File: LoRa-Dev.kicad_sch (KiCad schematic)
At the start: 14 parts, among them J2 Barrel_Jack_MountingPin, U1 RPi Pico, U2 LT1963AEQ

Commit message: board layout
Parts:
- added C3: 47uF, Capacitor_SMD:CP_Elec_6.3x5.8, symbol Device:C_Polarized_Small
- added C4: 0.1uF, Capacitor_SMD:C_0603_1608Metric, symbol Device:C_Small
- added J1: Conn_Coaxial_Small, Connector_Coaxial:U.FL_Hirose_U.FL-R-SMT-1_Vertical, symbol Connector:Conn_Coaxial_Small
- added R9: R_Small, Resistor_SMD:R_0603_1608Metric, symbol Device:R_Small
- added U3: LoRa126XF30, LoRa-Dev:LoRa126XF30, symbol LoRa-Dev:LoRa126XF30
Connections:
- net GND: now also J2.MP (MountPin), C3.2, C4.2, R9.2, U3.2 (GND), U3.8 (GND)
- net RF_VDD: now also C3.1, C4.1, U3.1 (VCC)
- net SPI_CSn: now also U3.7 (NSS)
- net SPI_MISO: now also U3.10 (MISO)
- net SPI_MOSI: now also U3.11 (MOSI)
- net SPI_SCK: now also U3.9 (SCK)
- net 12V: now reaches J2.1, R1.1, R2.1, R3.1, R4.1, R5.1, R6.1
- net DIO3: now reaches U1.26 (GP20)
- net DIO3: now also U3.14 (DIO3)
- net DIO1: now reaches U1.27 (GP21)
- net DIO1: now also U3.13 (DIO1)
- net RESETn: now reaches U1.29 (GP22)
- net RESETn: now also U3.5 (NRESET)
- net BUSY: now reaches U1.31 (GP26)
- net BUSY: now also U3.6 (BUSY)
- new net ANT: J1.1 (In), U3.16 (ANT)
- new net RF_GND: J1.2 (Ext), R9.1, U3.15 (GND)
- no-connect marks 0 -> 3

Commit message: RFM95W
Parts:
- removed C3: 47uF, Capacitor_SMD:CP_Elec_6.3x5.8, symbol Device:C_Polarized_Small
- removed C4: 0.1uF, Capacitor_SMD:C_0603_1608Metric, symbol Device:C_Small
- removed U3: LoRa126XF30, LoRa-Dev:LoRa126XF30, symbol LoRa-Dev:LoRa126XF30
- added C3: 0.1uF, Capacitor_SMD:C_0603_1608Metric, symbol Device:C_Small
- added C4: 47uF, Capacitor_SMD:CP_Elec_6.3x5.8, symbol Device:C_Polarized_Small
- added U5: RFM95W-868S2, LoRa-Dev:RFM95W, symbol RF_Module:RFM95W-868S2
- R7: value 1k5 -> 2K2
- R8: value 4k7 -> 1K2
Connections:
- net ANT: now also U5.9 (ANT)
- net DIO1: now also U5.15 (DIO1)
- net GND: now also C3.2, C4.2, U5.1 (GND), U5.10 (GND), U5.8 (GND)
- net RESETn: now also U5.6 (RESET)
- net RF_VDD: now also C3.1, C4.1, U5.13 (3.3V)
- net SPI_CSn: now also U5.5 (NSS)
- net SPI_MISO: now also U5.2 (MISO)
- net SPI_MOSI: now also U5.3 (MOSI)
- net SPI_SCK: now also U5.4 (SCK)
- net BUSY: no longer names the net of U1.31 (GP26)
- net DIO3 renamed DIO0
- net DIO0: now also U5.14 (DIO0)
- no-connect marks 3 -> 4

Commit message: RFM95PW wrong branch name
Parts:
- removed J1: Conn_Coaxial_Small, Connector_Coaxial:U.FL_Hirose_U.FL-R-SMT-1_Vertical, symbol Connector:Conn_Coaxial_Small
- removed U5: RFM95W-868S2, LoRa-Dev:RFM95W, symbol RF_Module:RFM95W-868S2
- added J3: Conn_Coaxial_Small, Connector_Coaxial:U.FL_Hirose_U.FL-R-SMT-1_Vertical, symbol Connector:Conn_Coaxial_Small
- added U3: RFM95PW, LoRa-Dev:RFM95PW, symbol LoRa-Dev:RFM95PW
- R7: value 2K2 -> 4k7
- R8: value 1K2 -> 1K5
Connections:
- net ANT: now also J3.1 (In), U3.1 (ANT)
- net DIO0: now also U3.6 (DIO0)
- net DIO1: now also U3.7 (DIO1)
- net GND: now also U3.16 (GND), U3.17 (GND), U3.2 (GND)
- net RESETn: now also U3.14 (RESET)
- net RF_GND: now also J3.2 (Ext)
- net RF_VDD: now also U3.5 (VCC)
- net SPI_CSn: now also U3.13 (NSS)
- net SPI_MISO: now also U3.10 (MISO)
- net SPI_MOSI: now also U3.11 (MOSI)
- net SPI_SCK: now also U3.12 (SCK)
- no-connect marks 4 -> 5
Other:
- moved on the sheet: R9

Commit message: E22-900M30S
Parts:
- removed C3: 0.1uF, Capacitor_SMD:C_0603_1608Metric, symbol Device:C_Small
- removed C4: 47uF, Capacitor_SMD:CP_Elec_6.3x5.8, symbol Device:C_Polarized_Small
- removed J3: Conn_Coaxial_Small, Connector_Coaxial:U.FL_Hirose_U.FL-R-SMT-1_Vertical, symbol Connector:Conn_Coaxial_Small
- removed U3: RFM95PW, LoRa-Dev:RFM95PW, symbol LoRa-Dev:RFM95PW
- added C5: 0.1uF, Capacitor_SMD:C_0603_1608Metric, symbol Device:C_Small
- added C6: 47uF, Capacitor_SMD:CP_Elec_6.3x5.8, symbol Device:C_Polarized_Small
- added J1: Conn_Coaxial_Small, Connector_Coaxial:U.FL_Hirose_U.FL-R-SMT-1_Vertical, symbol Connector:Conn_Coaxial_Small
- added U4: E22-900M30S-SX1262, LoRa-Dev:E22-900M30S-SX1262, symbol LoRa-Dev:E22-900M30S-SX1262
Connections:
- net ANT: now also J1.1 (In), U4.21 (ANT)
- net DIO1: now also U4.13 (DIO1)
- net GND: now also C5.2, C6.2, U4.1 (GND), U4.11 (GND), U4.12 (GND), U4.2 (GND), U4.20 (GND), U4.22 (GND), U4.3 (GND), U4.4 (GND), U4.5 (GND)
- net RESETn: now also U4.15 (NRST)
- net RF_GND: now also J1.2 (Ext)
- net RF_VDD: now also C5.1, C6.1, U4.10 (VCC), U4.9 (VCC)
- net SPI_CSn: now also U4.19 (NSS)
- net SPI_MISO: now also U4.16 (MISO)
- net SPI_MOSI: now also U4.17 (MOSI)
- net SPI_SCK: now also U4.18 (SCK)
- net BUSY: now reaches U1.31 (GP26)
- net BUSY: now also U4.14 (BUSY)
- net RXEN: now reaches U1.32 (GP27)
- net RXEN: now also U4.6 (RXEN)
- net TXEN: now reaches U1.34 (GP28)
- net TXEN: now also U4.7 (TXEN)
- net DIO0 renamed DIO2
- net DIO2: now also U4.8 (DIO2)
- no-connect marks 5 -> 0

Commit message: updated after first review
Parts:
- removed C6: 47uF, Capacitor_SMD:CP_Elec_6.3x5.8, symbol Device:C_Polarized_Small
- added C3: 47uf, Capacitor_SMD:C_1210_3225Metric, symbol Device:C_Small
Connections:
- net GND: now also C3.2; no longer U4.1 (GND), U4.2 (GND), U4.20 (GND), U4.22 (GND), U4.3 (GND)
- net RF_GND: now also U4.1 (GND), U4.2 (GND), U4.20 (GND), U4.22 (GND), U4.3 (GND)
- net RF_VDD: now also C3.1
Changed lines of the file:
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@@
 	(wire
 		(pts
+			(xy 182.88 74.93) (xy 182.88 82.55)
+		)
+		(stroke
+			(width 0)
+			(type default)
+		)
+	)
+	(wire
+		(pts
 			(xy 193.04 69.85) (xy 207.01 69.85)
 		)
@@
 	(wire
 		(pts
-			(xy 152.4 54.61) (xy 158.75 54.61)
+			(xy 151.13 54.61) (xy 158.75 54.61)
 		)
 		(stroke
@@
 	(wire
 		(pts
-			(xy 152.4 57.15) (xy 158.75 57.15)
+			(xy 151.13 57.15) (xy 158.75 57.15)
 		)
 		(stroke
@@
 	(wire
 		(pts
-			(xy 152.4 62.23) (xy 158.75 62.23)
+			(xy 224.79 67.31) (xy 224.79 71.12)
 		)
 		(stroke
@@
 	(wire
 		(pts
-			(xy 224.79 67.31) (xy 224.79 71.12)
+			(xy 152.4 62.23) (xy 158.75 62.23)
 		)
 		(stroke
@@
 	(wire
 		(pts
-			(xy 152.4 52.07) (xy 158.75 52.07)
+			(xy 236.22 67.31) (xy 236.22 71.12)
 		)
 		(stroke
@@
 	(wire
 		(pts
-			(xy 236.22 67.31) (xy 236.22 71.12)
+			(xy 148.59 135.89) (xy 154.94 135.89)
 		)
 		(stroke
@@
 	(wire
 		(pts
-			(xy 148.59 135.89) (xy 154.94 135.89)
+			(xy 177.8 74.93) (xy 177.8 82.55)
+		)
+		(stroke
+			(width 0)
+			(type default)
+		)
+	)
+	(wire
+		(pts
+			(xy 151.13 52.07) (xy 158.75 52.07)
 		)
 		(stroke
@@
 	(wire
 		(pts
-			(xy 152.4 62.23) (xy 152.4 62.2498)
-		)
-		(stroke
-			(width 0)
-			(type default)
-		)
-	)
-	(wire
-		(pts
 			(xy 267.97 39.37) (xy 256.54 39.37)
 		)
@@
 	(wire
 		(pts
-			(xy 182.88 74.93) (xy 182.88 81.28)
-		)
-		(stroke
-			(width 0)
-			(type default)
-		)
-	)
-	(wire
-		(pts
 			(xy 104.14 146.05) (xy 104.14 149.86)
 		)
@@
 	(wire
 		(pts
-			(xy 177.8 74.93) (xy 177.8 81.28)
-		)
-		(stroke
-			(width 0)
-			(type default)
-		)
-	)
-	(wire
-		(pts
 			(xy 34.29 91.44) (xy 45.72 91.44)
 		)
@@
 		)
 	)
+	(label "RF_GND"
+		(at 177.8 82.55 90)
+		(fields_autoplaced yes)
+		(effects
+			(font
+				(size 1.27 1.27)
+			)
+			(justify left bottom)
+		)
+	)
 	(label "RXEN"
 		(at 81.28 68.58 0)
@@
 		)
 	)
-	(label "GND"
-		(at 182.88 80.01 90)
+	(label "RF_GND"
+		(at 151.13 54.61 0)
 		(fields_autoplaced yes)
 		(effects
@@
 	)
 	(label "GND"
-		(at 157.48 54.61 180)
+		(at 198.12 64.77 180)
 		(fields_autoplaced yes)
 		(effects
@@
 		)
 	)
-	(label "GND"
-		(at 198.12 64.77 180)
+	(label "RF_GND"
+		(at 151.13 52.07 0)
 		(fields_autoplaced yes)
 		(effects
@@
 				(size 1.27 1.27)
 			)
-			(justify right bottom)
+			(justify left bottom)
 		)
 	)
@@
 	)
 	(label "GND"
-		(at 157.48 57.15 180)
+		(at 78.74 66.04 0)
 		(fields_autoplaced yes)
 		(effects
@@
 				(size 1.27 1.27)
 			)
-			(justify right bottom)
+			(justify left bottom)
 		)
 	)
-	(label "GND"
-		(at 78.74 66.04 0)
+	(label "RF_GND"
+		(at 182.88 82.55 90)
 		(fields_autoplaced yes)
 		(effects
@@
 	)
 	(label "GND"
-		(at 157.48 52.07 180)
-		(fields_autoplaced yes)
-		(effects
-			(font
-				(size 1.27 1.27)
-			)
-			(justify right bottom)
-		)
-	)
-	(label "GND"
 		(at 267.97 39.37 180)
 		(fields_autoplaced yes)
@@
 		)
 	)
-	(label "GND"
-		(at 157.48 62.23 180)
-		(fields_autoplaced yes)
-		(effects
-			(font
-				(size 1.27 1.27)
-			)
-			(justify right bottom)
-		)
-	)
 	(label "SPI_MOSI"
 		(at 170.18 77.47 270)
@@
 		)
 	)
-	(label "GND"
-		(at 177.8 80.01 90)
-		(fields_autoplaced yes)
-		(effects
-			(font
-				(size 1.27 1.27)
-			)
-			(justify left bottom)
-		)
-	)
 	(label "SPI_SCK"
 		(at 78.74 88.9 0)
@@
 		)
 	)
+	(label "RF_GND"
+		(at 151.13 57.15 0)
+		(fields_autoplaced yes)
+		(effects
+			(font
+				(size 1.27 1.27)
+			)
+			(justify left bottom)
+		)
+	)
 	(label "TXEN"
 		(at 153.67 67.31 0)
@@
 	)
 	(label "GND"
+		(at 157.48 62.23 180)
+		(fields_autoplaced yes)
+		(effects
+			(font
+				(size 1.27 1.27)
+			)
+			(justify right bottom)
+		)
+	)
+	(label "GND"
 		(at 198.12 62.23 180)
 		(fields_autoplaced yes)
@@
 	)
 	(symbol
+		(lib_id "Device:C_Small")
+		(at 236.22 73.66 0)
+		(unit 1)
+		(exclude_from_sim no)
+		(in_bom yes)
+		(on_board yes)
+		(dnp no)
+		(fields_autoplaced yes)
+		(property "Reference" "C3"
+			(at 238.76 72.3962 0)
+			(effects
+				(font
+					(size 1.27 1.27)
+				)
+				(justify left)
+			)
+		)
+		(property "Value" "47uf"
+			(at 238.76 74.9362 0)
+			(effects
+				(font
+					(size 1.27 1.27)
+				)
+				(justify left)
+			)
+		)
+		(property "Footprint" "Capacitor_SMD:C_1210_3225Metric"
+			(at 236.22 73.66 0)
+			(effects
+				(font
+					(size 1.27 1.27)
+				)
+				(hide yes)
+			)
+		)
+		(property "Datasheet" "~"
+			(at 236.22 73.66 0)
+			(effects
+				(font
+					(size 1.27 1.27)
+				)
+				(hide yes)
+			)
+		)
+		(property "Description" "Unpolarized capacitor, small symbol"
+			(at 236.22 73.66 0)
+			(effects
+				(font
+					(size 1.27 1.27)
+				)
+				(hide yes)
+			)
+		)
+		(pin "2"
+		)
+		(pin "1"
+		)
+		(instances
+			(project "LoRa-Dev"
+				(path "/ef1cdc4e-4ca4-4643-8589-6d5225afae9e"
+					(reference "C3")
+					(unit 1)
+				)
+			)
+		)
+	)
+	(symbol
 		(lib_id "Device:R_Small")
 		(at 66.04 140.97 90)
@@
 					(unit 1)
 				)
-			)
-		)
-	)
-	(symbol
-		(lib_id "Device:C_Polarized_Small")
-		(at 236.22 73.66 0)
-		(unit 1)
-		(exclude_from_sim no)
-		(in_bom yes)
-		(on_board yes)
-		(dnp no)
-		(fields_autoplaced yes)
-		(property "Reference" "C6"
-			(at 238.76 71.8438 0)
-			(effects
-				(font
-					(size 1.27 1.27)
-				)
-				(justify left)
-			)
-		)
-		(property "Value" "47uF"
-			(at 238.76 74.3838 0)
-			(effects
-				(font
-					(size 1.27 1.27)
-				)
-				(justify left)
-			)
-		)
-		(property "Footprint" "Capacitor_SMD:CP_Elec_6.3x5.8"
-			(at 236.22 73.66 0)
-			(effects
-				(font
-					(size 1.27 1.27)
-				)
-				(hide yes)
-			)
-		)
-		(property "Datasheet" "~"
-			(at 236.22 73.66 0)
-			(effects
-				(font
-					(size 1.27 1.27)
-				)
-				(hide yes)
-			)
-		)
-		(property "Description" "Polarized capacitor, small symbol"
-			(at 236.22 73.66 0)
-			(effects
-				(font
-					(size 1.27 1.27)
-				)
-				(hide yes)
-			)
-		)
-		(pin "1"
-		)
-		(pin "2"
-		)
-		(instances
-			(project "LoRa-Dev"
-				(path "/ef1cdc4e-4ca4-4643-8589-6d5225afae9e"
-					(reference "C6")
-					(unit 1)
-				)

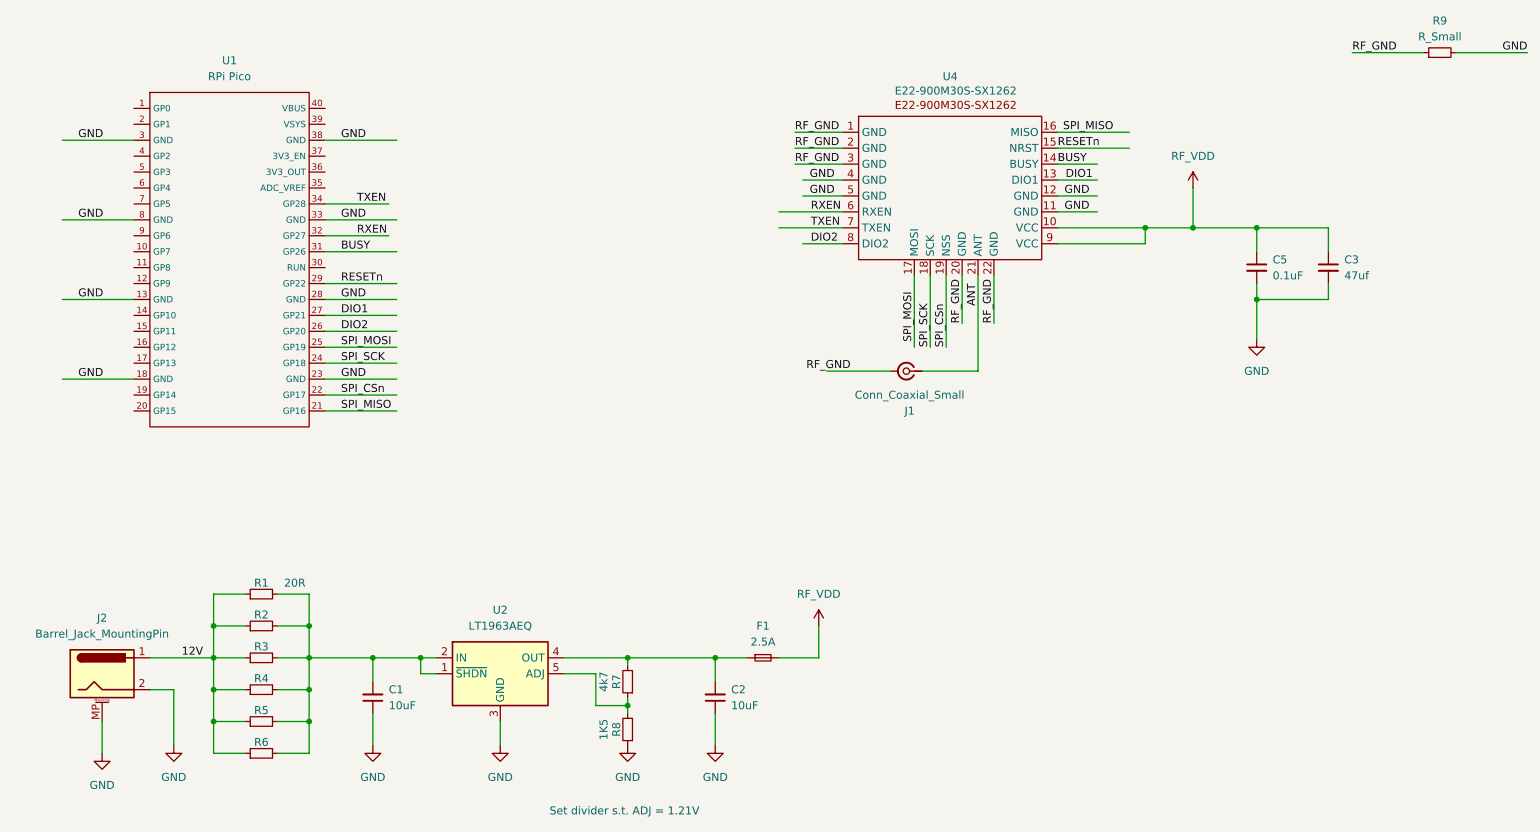
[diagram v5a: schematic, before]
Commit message: Some fixes, exported BOM
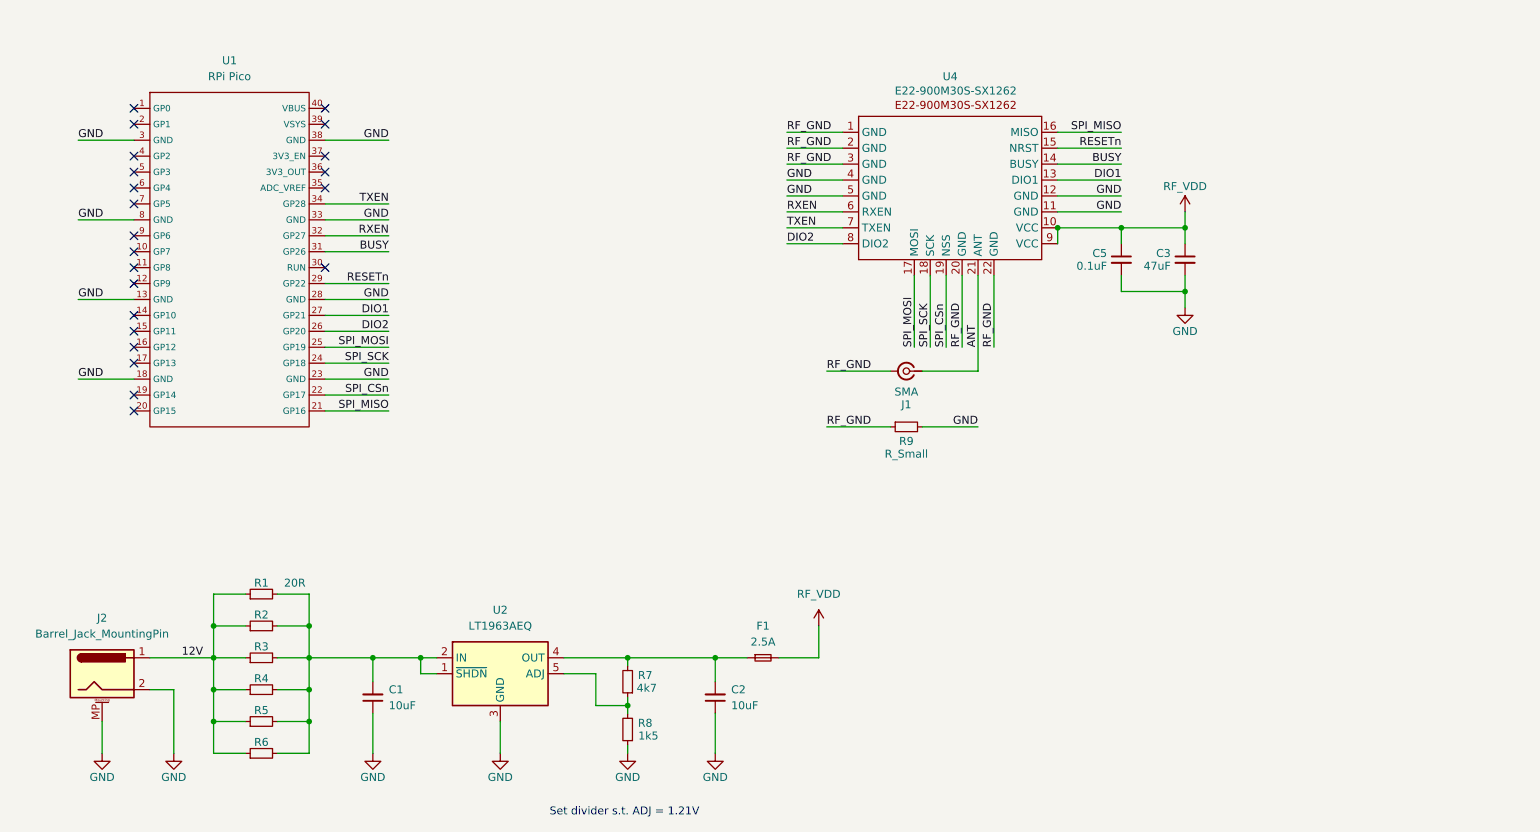
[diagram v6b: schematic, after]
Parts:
- C3: value 47uf -> 47uF
- J1: value Conn_Coaxial_Small -> SMA; footprint Connector_Coaxial:U.FL_Hirose_U.FL-R-SMT-1_Vertical -> Connector_Coaxial:SMA_Amphenol_901-144_Vertical
- R8: value 1K5 -> 1k5
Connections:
- no-connect marks 0 -> 22
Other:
- moved on the sheet: C3, C5, R9
